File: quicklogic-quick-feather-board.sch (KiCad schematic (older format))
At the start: 81 parts, among them IC1 EOS-S3, J1 SHF-105-01-L-D-SM, J2 1x12_pinhead, J3 1x16_pinhead, J5 0473460001, Q1 BSS138AKA, Q2 BSS84, U1 TPS62821DLCR, U2 MCP73831T-2ACI_OT, U3 GD25Q16CWIGR, U4 DPS310, U5 MC3635, X1 ECS-_327-12_5-34B-TR

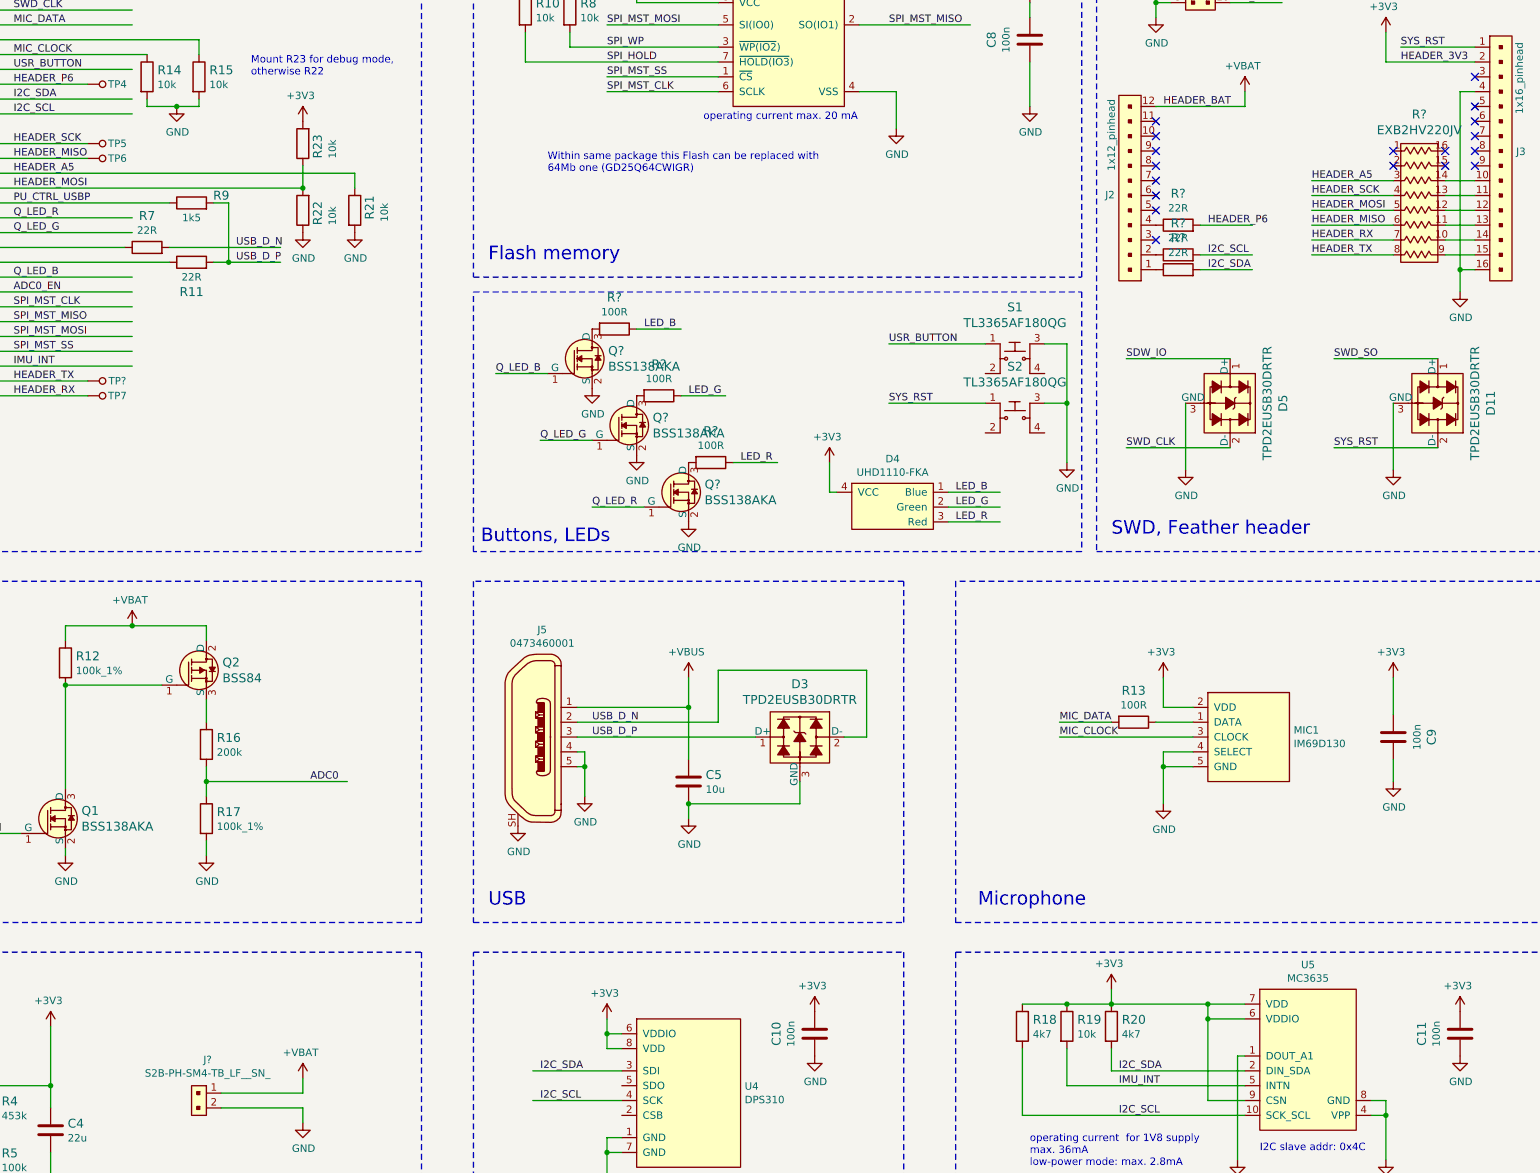
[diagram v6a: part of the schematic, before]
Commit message: Updated schematic annotation
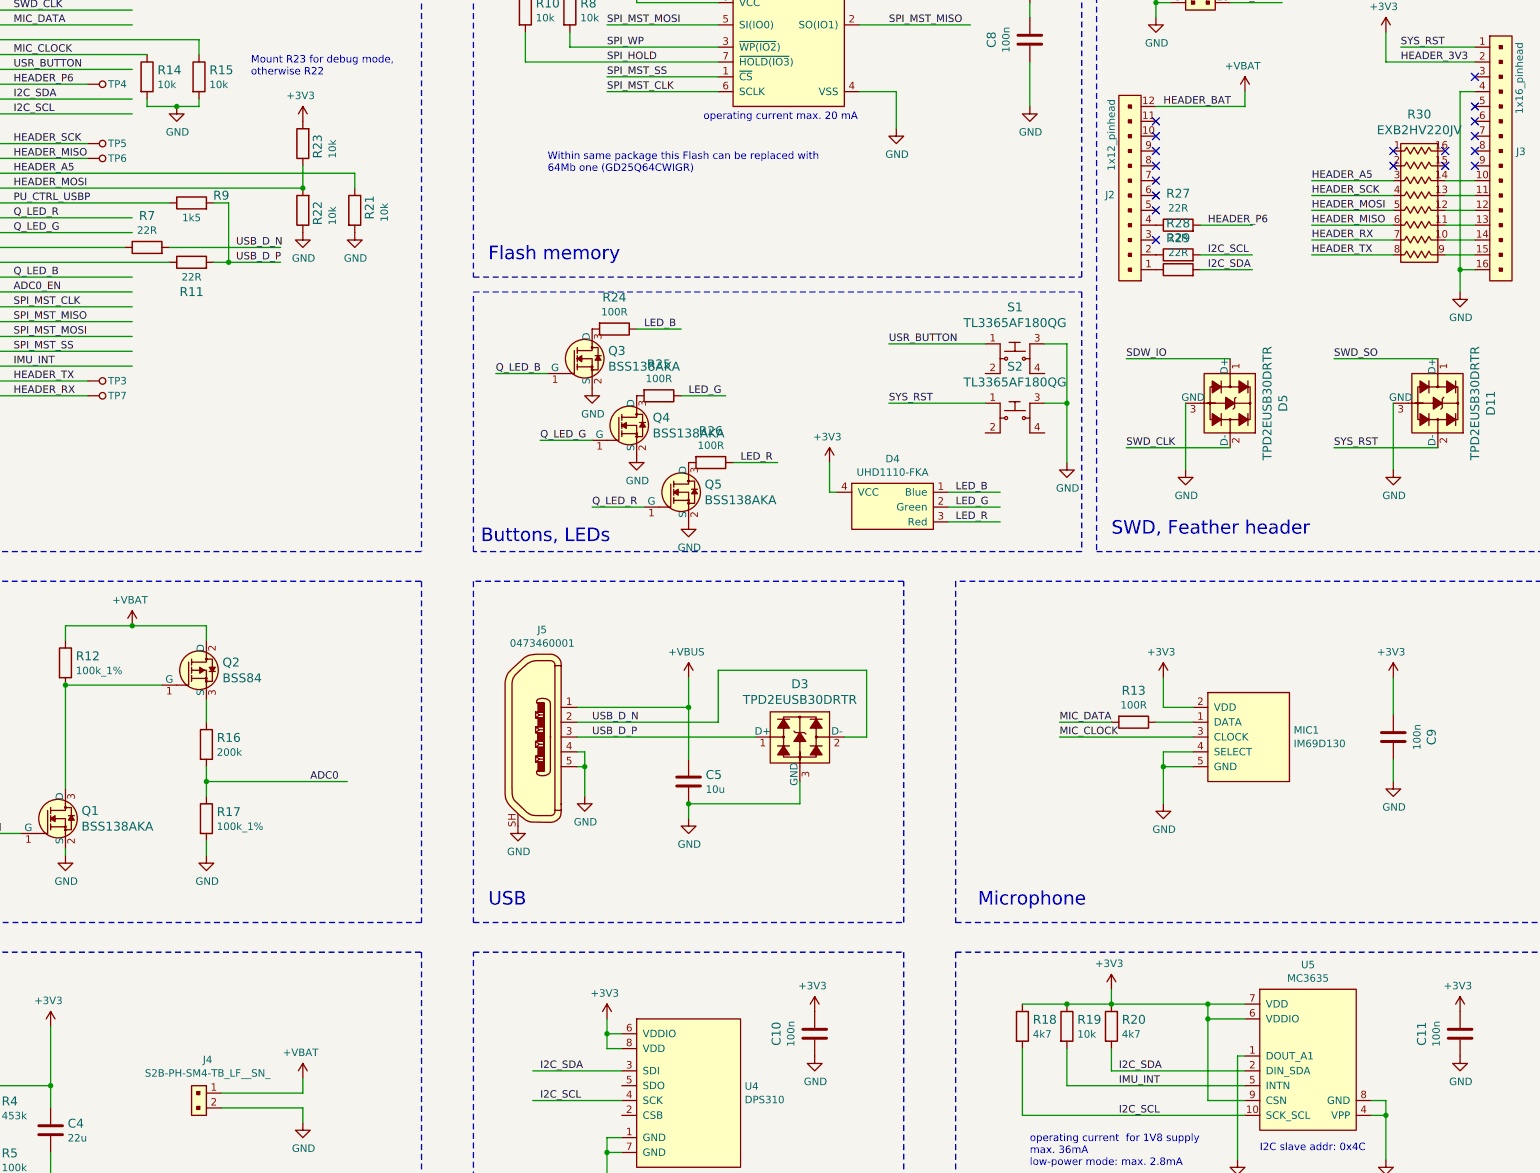
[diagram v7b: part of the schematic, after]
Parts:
- gave numbers to parts that had none: 12
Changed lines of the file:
@@
 	13450 6350 13250 6350
 $Comp
-L quicklogic-quick-feather-board:GND #PWR?
+L quicklogic-quick-feather-board:GND #PWR027
 U 1 1 5DF37EEC
 P 10050 5100
-F 0 "#PWR?" H 10050 4850 50  0001 C CNN
+F 0 "#PWR027" H 10050 4850 50  0001 C CNN
 F 1 "GND" H 10055 4927 50  0000 C CNN
 F 2 "" H 10050 5100 50  0001 C CNN
@@
 $EndComp
 $Comp
-L quicklogic-quick-feather-board:GND #PWR?
+L quicklogic-quick-feather-board:GND #PWR026
 U 1 1 5DF38279
 P 9700 4650
-F 0 "#PWR?" H 9700 4400 50  0001 C CNN
+F 0 "#PWR026" H 9700 4400 50  0001 C CNN
 F 1 "GND" H 9705 4477 50  0000 C CNN
 F 2 "" H 9700 4650 50  0001 C CNN
@@
 $EndComp
 $Comp
-L quicklogic-quick-feather-board:GND #PWR?
+L quicklogic-quick-feather-board:GND #PWR025
 U 1 1 5DF3863F
 P 9400 4200
-F 0 "#PWR?" H 9400 3950 50  0001 C CNN
+F 0 "#PWR025" H 9400 3950 50  0001 C CNN
 F 1 "GND" H 9405 4027 50  0000 C CNN
 F 2 "" H 9400 4200 50  0001 C CNN
@@
 LED_R
 $Comp
-L quicklogic-quick-feather-board:R_100R_0402 R?
+L quicklogic-quick-feather-board:R_100R_0402 R26
 U 1 1 5E02513F
 P 10200 4700
-F 0 "R?" H 10200 4487 60  0000 C CNN
+F 0 "R26" H 10200 4487 60  0000 C CNN
 F 1 "R_100R_0402" H 10200 4550 60  0001 C CNN
 F 2 "quicklogic-quick-feather-board-footprints:0402-res" H 10400 4900 60  0001 L CNN
@@
 $EndComp
 $Comp
-L quicklogic-quick-feather-board:R_100R_0402 R?
+L quicklogic-quick-feather-board:R_100R_0402 R25
 U 1 1 5E0259C0
 P 9850 4250
-F 0 "R?" H 9850 4037 60  0000 C CNN
+F 0 "R25" H 9850 4037 60  0000 C CNN
 F 1 "R_100R_0402" H 9850 4100 60  0001 C CNN
 F 2 "quicklogic-quick-feather-board-footprints:0402-res" H 10050 4450 60  0001 L CNN
@@
 $EndComp
 $Comp
-L quicklogic-quick-feather-board:R_100R_0402 R?
+L quicklogic-quick-feather-board:R_100R_0402 R24
 U 1 1 5E026C5D
 P 9550 3800
-F 0 "R?" H 9550 3587 60  0000 C CNN
+F 0 "R24" H 9550 3587 60  0000 C CNN
 F 1 "R_100R_0402" H 9550 3650 60  0001 C CNN
 F 2 "quicklogic-quick-feather-board-footprints:0402-res" H 9750 4000 60  0001 L CNN
@@
 Q_LED_B
 $Comp
-L quicklogic-quick-feather-board:BSS138AKA Q?
+L quicklogic-quick-feather-board:BSS138AKA Q3
 U 1 1 5E1733EE
 P 9400 4000
-F 0 "Q?" H 9508 4053 60  0000 L CNN
+F 0 "Q3" H 9508 4053 60  0000 L CNN
 F 1 "BSS138AKA" H 9508 3947 60  0000 L CNN
 F 2 "quicklogic-quick-feather-board-footprints:SOT-23-3" H 9600 4200 60  0001 L CNN
@@
 $EndComp
 $Comp
-L quicklogic-quick-feather-board:BSS138AKA Q?
+L quicklogic-quick-feather-board:BSS138AKA Q4
 U 1 1 5E1749E3
 P 9700 4450
-F 0 "Q?" H 9808 4503 60  0000 L CNN
+F 0 "Q4" H 9808 4503 60  0000 L CNN
 F 1 "BSS138AKA" H 9808 4397 60  0000 L CNN
 F 2 "quicklogic-quick-feather-board-footprints:SOT-23-3" H 9900 4650 60  0001 L CNN
@@
 $EndComp
 $Comp
-L quicklogic-quick-feather-board:BSS138AKA Q?
+L quicklogic-quick-feather-board:BSS138AKA Q5
 U 1 1 5E174FE9
 P 10050 4900
-F 0 "Q?" H 10158 4953 60  0000 L CNN
+F 0 "Q5" H 10158 4953 60  0000 L CNN
 F 1 "BSS138AKA" H 10158 4847 60  0000 L CNN
 F 2 "quicklogic-quick-feather-board-footprints:SOT-23-3" H 10250 5100 60  0001 L CNN
@@
 	5250 2050 6300 2050
 $Comp
-L quicklogic-quick-feather-board:TP_SMD1MM TP?
+L quicklogic-quick-feather-board:TP_SMD1MM TP3
 U 1 1 5E2DB6B4
 P 6100 4150
-F 0 "TP?" V 6100 4050 50  0000 C CNN
+F 0 "TP3" V 6100 4050 50  0000 C CNN
 F 1 "TP_SMD1MM" H 6100 4050 50  0001 C CNN
 F 2 "quicklogic-quick-feather-board-footprints:Testpoint_smd_1mm" H 6300 4350 60  0001 L CNN
@@
 NoConn ~ 13200 3200
 $Comp
-L antmicroRectangularConnectorsHeadersMalePins:S2B-PH-SM4-TB_LF__SN_ J?
+L antmicroRectangularConnectorsHeadersMalePins:S2B-PH-SM4-TB_LF__SN_ J4
 U 1 1 5E3F3FA2
 P 6800 8950
-F 0 "J?" V 6575 8958 50  0000 C CNN
+F 0 "J4" V 6575 8958 50  0000 C CNN
 F 1 "S2B-PH-SM4-TB_LF__SN_" V 6666 8958 50  0000 C CNN
 F 2 "antmicro-footprints:PinHeader_2x1mm_P2mm_SMD_RA" H 7000 9150 60  0001 L CNN
@@
 $EndComp
 $Comp
-L quicklogic-quick-feather-board:+VBAT #PWR?
+L quicklogic-quick-feather-board:+VBAT #PWR023
 U 1 1 5E3F5F39
 P 7450 8800
-F 0 "#PWR?" H 7450 8800 50  0001 C CNN
+F 0 "#PWR023" H 7450 8800 50  0001 C CNN
 F 1 "+VBAT" H 7435 8923 50  0000 C CNN
 F 2 "" H 7450 8800 50  0001 C CNN
@@
 $EndComp
 $Comp
-L quicklogic-quick-feather-board:GND #PWR?
+L quicklogic-quick-feather-board:GND #PWR024
 U 1 1 5E3F6565
 P 7450 9150
-F 0 "#PWR?" H 7450 8900 50  0001 C CNN
+F 0 "#PWR024" H 7450 8900 50  0001 C CNN
 F 1 "GND" H 7455 8977 50  0000 C CNN
 F 2 "" H 7450 9150 50  0001 C CNN
@@
 	7450 8850 7450 8950
 $Comp
-L quicklogic-quick-feather-board:EXB2HV220JV R?
+L quicklogic-quick-feather-board:EXB2HV220JV R30
 U 1 1 5E56D4AE
 P 15000 3000
-F 0 "R?" H 14975 3647 60  0000 C CNN
+F 0 "R30" H 14975 3647 60  0000 C CNN
 F 1 "EXB2HV220JV" H 14975 3541 60  0000 C CNN
 F 2 "quicklogic-quick-feather-board-footprints:R_Array_Convex_8x0602" H 14800 3650 60  0001 L CNN
@@
 NoConn ~ 14800 2700
 $Comp
-L quicklogic-quick-feather-board:R_22R_0402 R?
+L quicklogic-quick-feather-board:R_22R_0402 R27
 U 1 1 5E71FDBA
 P 13350 3100
-F 0 "R?" H 13350 3313 60  0000 C CNN
+F 0 "R27" H 13350 3313 60  0000 C CNN
 F 1 "R_22R_0402" H 13350 2950 60  0001 C CNN
 F 2 "quicklogic-quick-feather-board-footprints:0402-res" H 13550 3300 60  0001 L CNN
@@
 $EndComp
 $Comp
-L quicklogic-quick-feather-board:R_22R_0402 R?
+L quicklogic-quick-feather-board:R_22R_0402 R28
 U 1 1 5E720B3F
 P 13350 3300
-F 0 "R?" H 13350 3513 60  0000 C CNN
+F 0 "R28" H 13350 3513 60  0000 C CNN
 F 1 "R_22R_0402" H 13350 3150 60  0001 C CNN
 F 2 "quicklogic-quick-feather-board-footprints:0402-res" H 13550 3500 60  0001 L CNN
@@
 $EndComp
 $Comp
-L quicklogic-quick-feather-board:R_22R_0402 R?
+L quicklogic-quick-feather-board:R_22R_0402 R29
 U 1 1 5E720ED0
 P 13350 3400
-F 0 "R?" H 13350 3613 60  0000 C CNN
+F 0 "R29" H 13350 3613 60  0000 C CNN
 F 1 "R_22R_0402" H 13350 3250 60  0001 C CNN
 F 2 "quicklogic-quick-feather-board-footprints:0402-res" H 13550 3600 60  0001 L CNN

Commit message: Added TBDs to schematics
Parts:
- removed J1: SHF-105-01-L-D-SM, quicklogic-quick-feather-board-footprints:SHF-105-01-L-D-SM, symbol quicklogic-quick-feather-board:SHF-105-01-L-D-SM
- removed Q3, Q4, Q5: BSS138AKA, quicklogic-quick-feather-board-footprints:SOT-23-3, symbol quicklogic-quick-feather-board:BSS138AKA
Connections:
- net labels added: SWD_IO
- wire segments 281 -> 269
- no-connect marks 20 -> 18
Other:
- note added: "TBD: Discuss on how to re-program the flash"
- note added: "TBD: check if we can fit in BOM with that"
- note added: "TBD: discuss LED driving circuit"
- moved on the sheet: R24, R25, R26
